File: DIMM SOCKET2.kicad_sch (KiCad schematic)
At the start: 6 parts, among them J5 DIMM REF

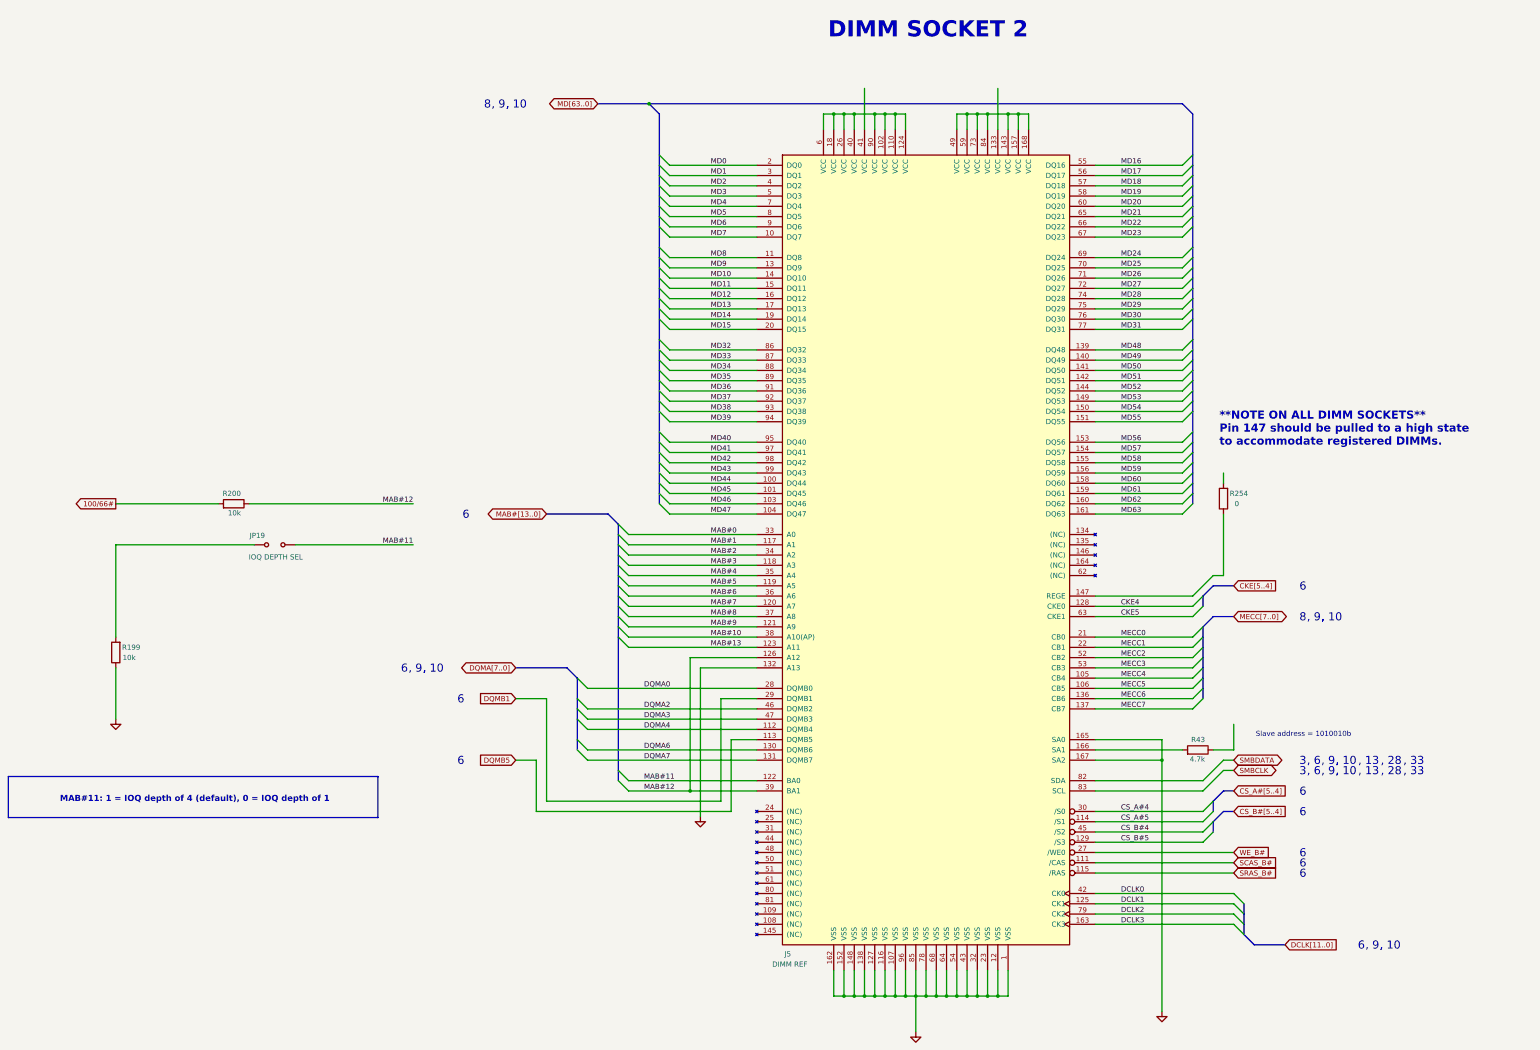
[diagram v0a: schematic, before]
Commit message: page 18 ISA, small fixes
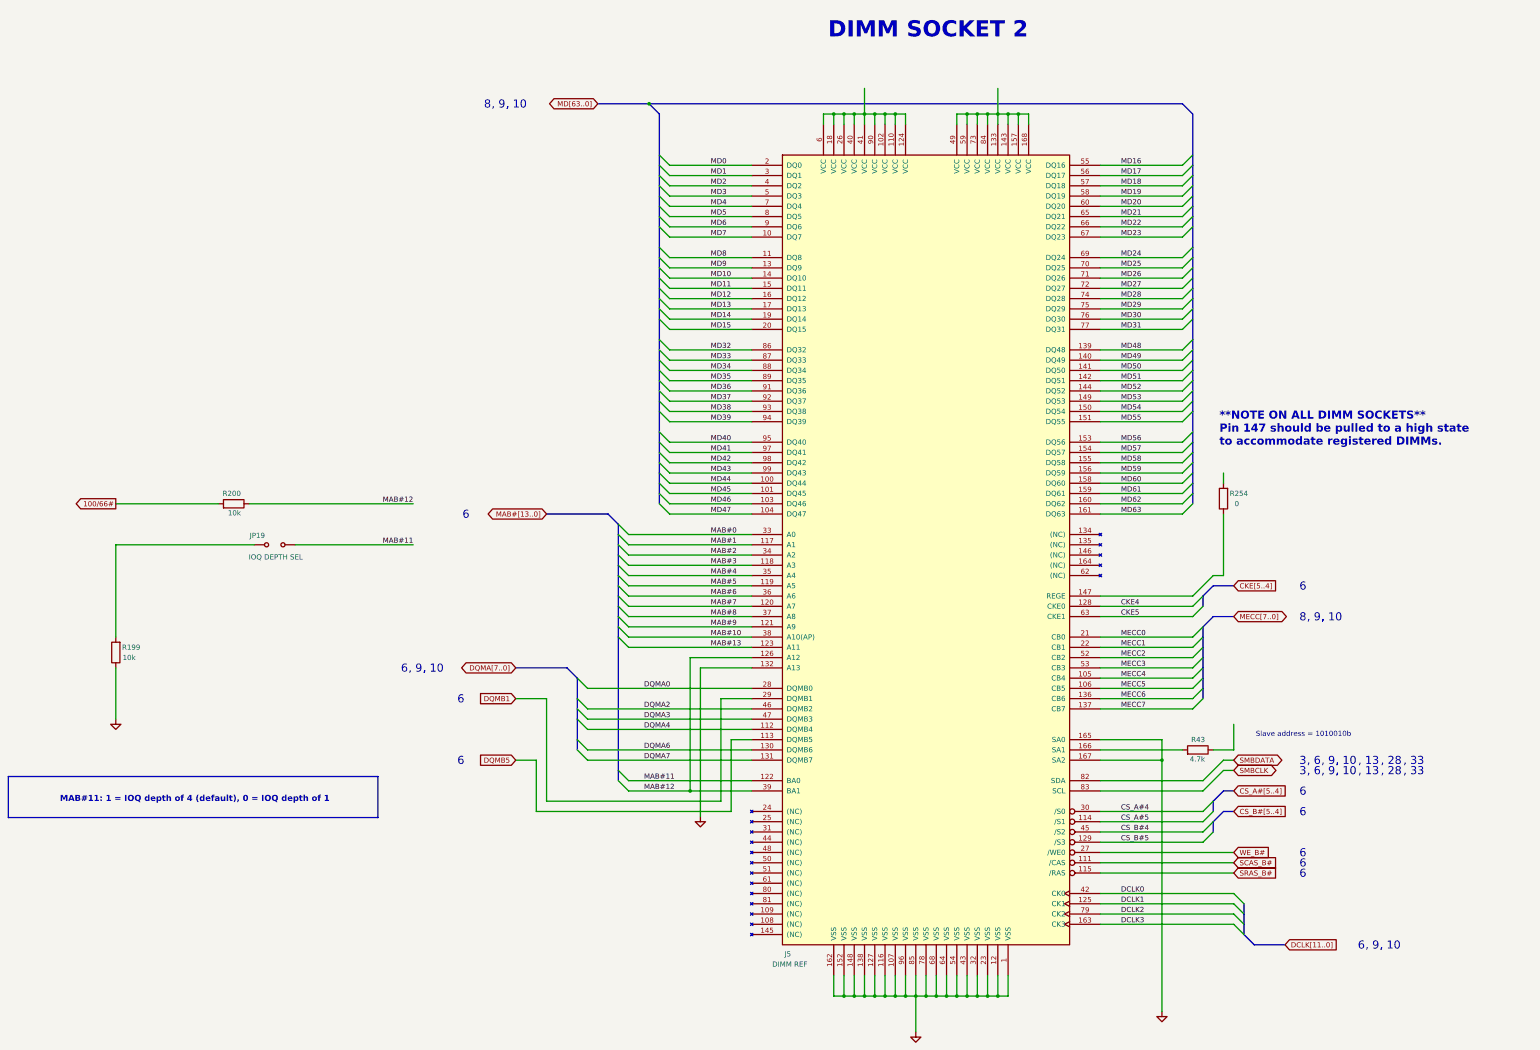
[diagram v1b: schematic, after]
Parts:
- J5: symbol P2-3_era:SDRAM_GENERIC -> P2-3_era:SDRAM_Slot
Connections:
- net at J5.102 (VCC), J5.110 (VCC), J5.124 (VCC)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: now also J5.41 (VCC)
- net at J5.133 (VCC): now also J5.143 (VCC), J5.157 (VCC), J5.168 (VCC), J5.49 (VCC), J5.59 (VCC), J5.73 (VCC), J5.84 (VCC)

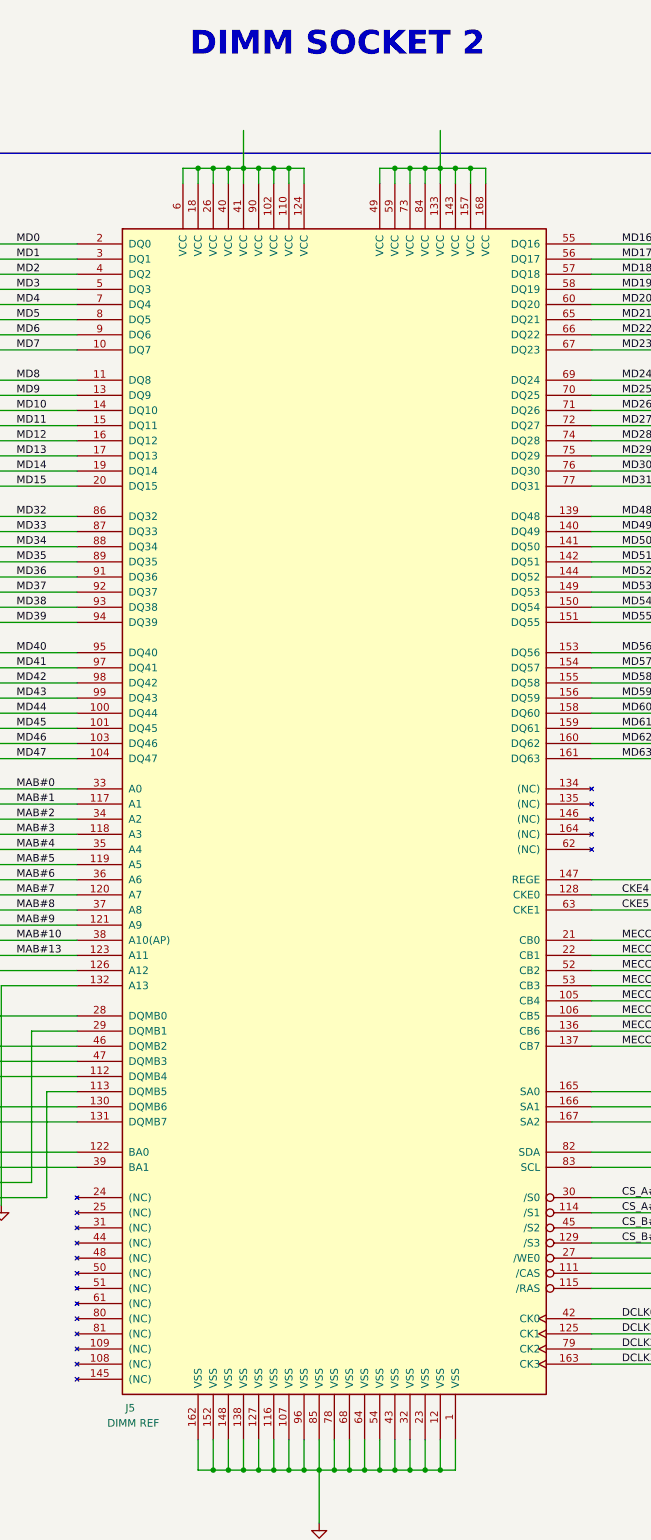
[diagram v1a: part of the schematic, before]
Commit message: page 6,7,8 82443BX chipset, various small fixes
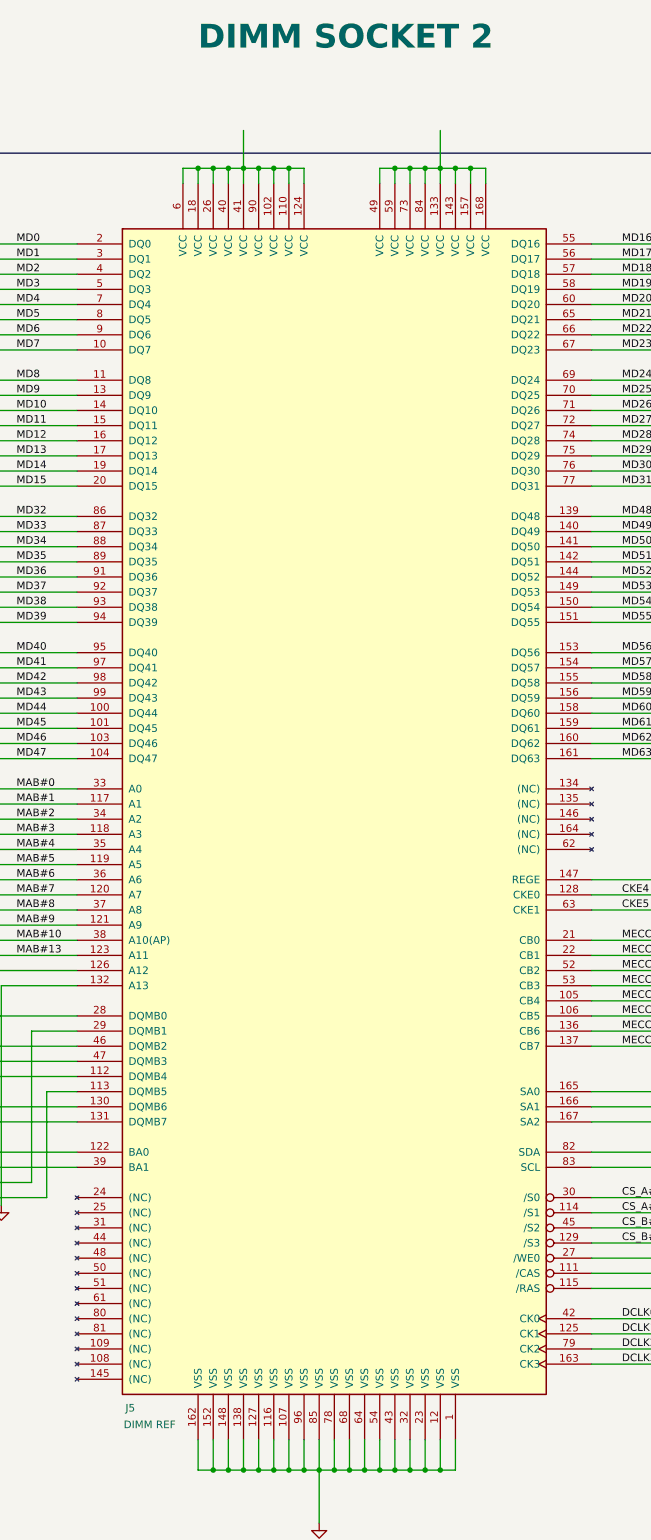
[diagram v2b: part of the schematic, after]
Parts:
- J5: value DIMM REF -> DIMM SOCKET 2
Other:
- note removed: "DIMM SOCKET 2"
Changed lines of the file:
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@@
 			(width 0.1303)
 			(type solid)
-			(color 0 0 0 1)
 		)
 		(fill
@@
 				(thickness 0.3)
 				(bold yes)
-				(color 0 0 0 1)
 			)
 		)
@@
 				(thickness 0.4)
 				(bold yes)
-				(color 0 0 0 1)
 			)
 			(justify left)
@@
 		)
 	)
-	(text "DIMM SOCKET 2"
-		(exclude_from_sim no)
-		(at 246.888 29.972 0)
-		(effects
-			(font
-				(size 4 4)
-				(thickness 0.8)
-				(bold yes)
-				(color 0 0 0 1)
-			)
-		)
-	)
 	(text "33"
 		(exclude_from_sim no)
@@
 			)
 		)
-		(property "Value" "DIMM REF"
-			(at 208.28 261.366 0)
+		(property "Value" "DIMM SOCKET 2"
+			(at 223.52 28.702 0)
 			(effects
 				(font
-					(size 1.27 1.27)
+					(size 4 4)
+					(thickness 0.8)
+					(bold yes)
 				)
 				(justify left)
@@
 			)
 		)
-		(property "Description" "DIMM SOCKET"
-			(at 248.158 186.69 0)
+		(property "Description" "DIMM REF"
+			(at 215.392 261.62 0)
 			(effects
 				(font
 					(size 1.27 1.27)
 				)
-				(hide yes)
 			)
 		)
